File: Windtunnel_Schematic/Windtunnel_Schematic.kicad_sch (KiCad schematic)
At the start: 8 parts

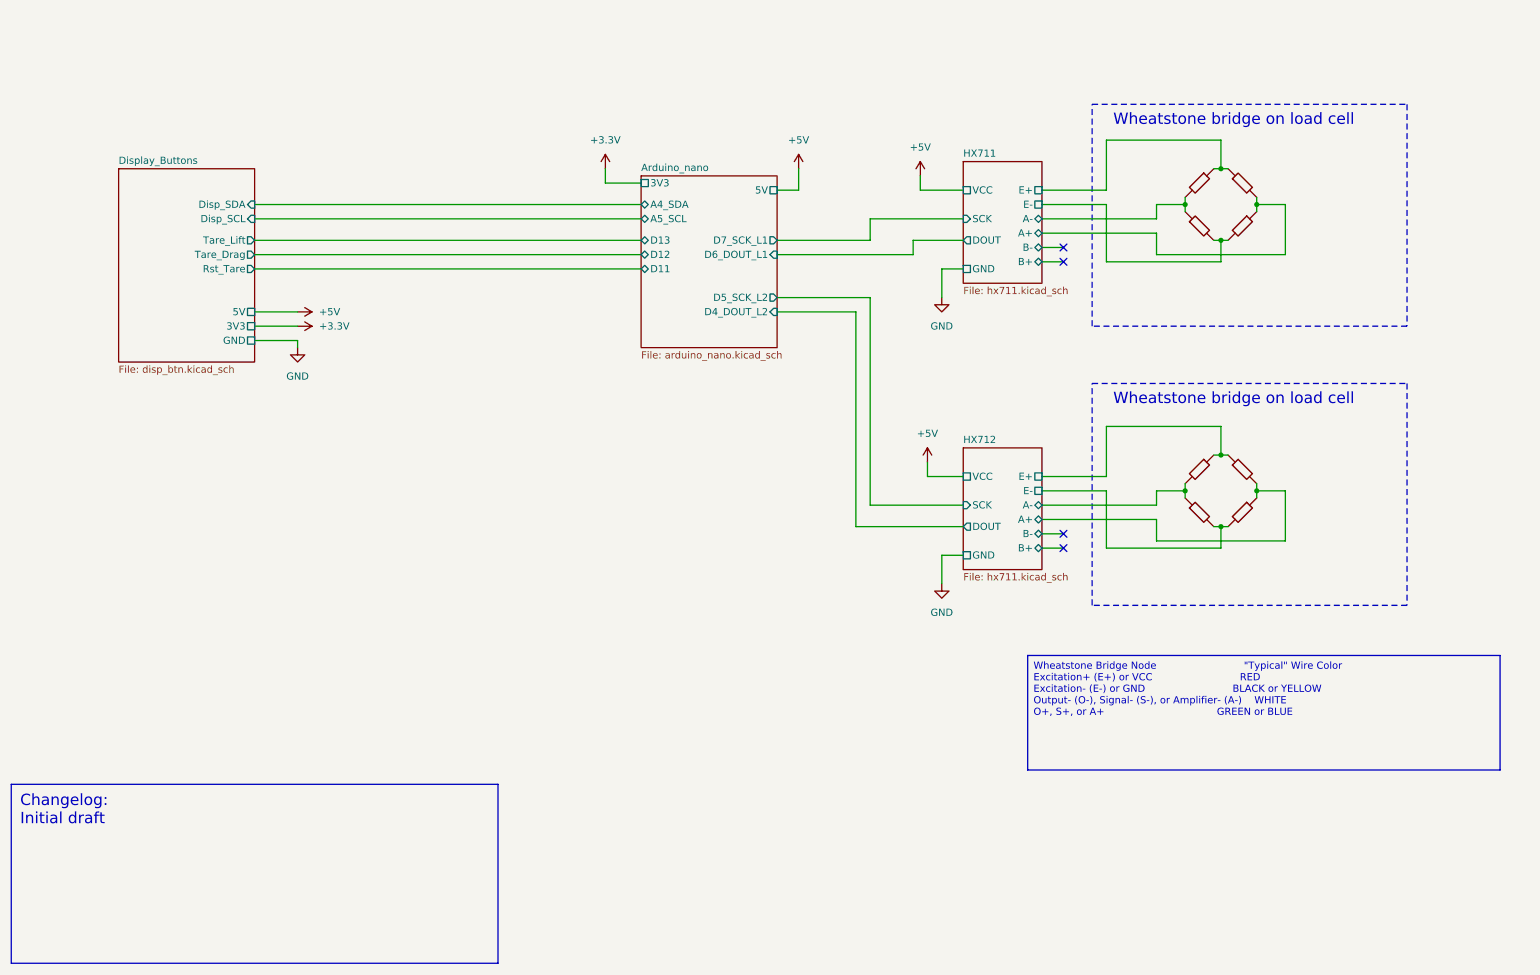
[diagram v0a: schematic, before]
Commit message: Added sub D9 and screw terminals
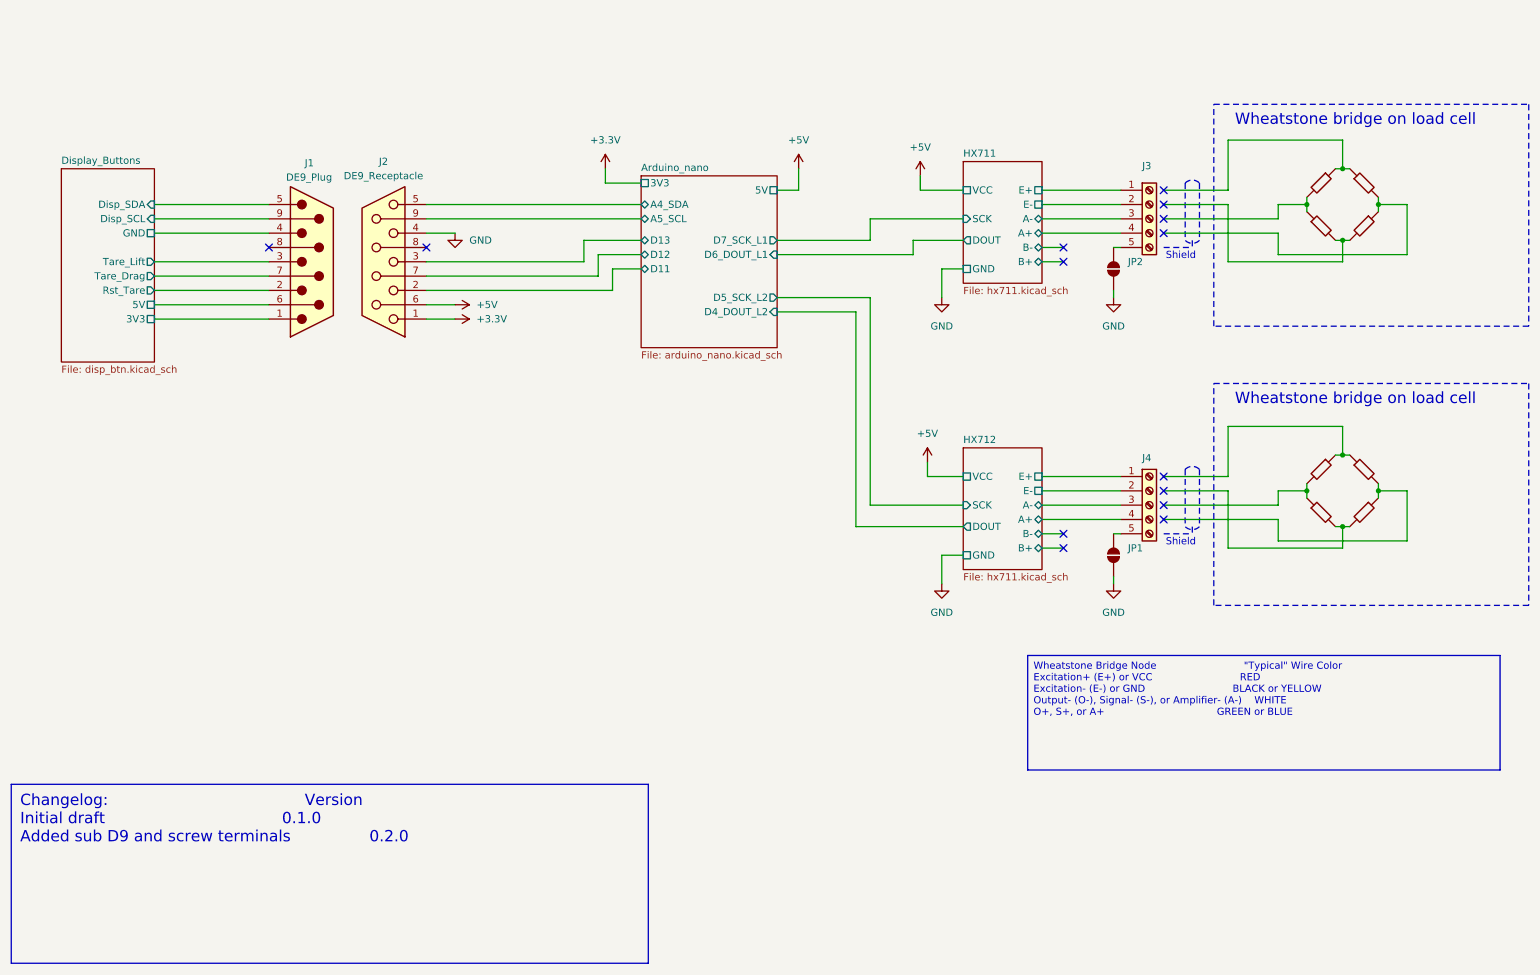
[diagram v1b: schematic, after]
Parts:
- added J1: DE9_Plug, symbol Connector:DE9_Plug
- added J2: DE9_Receptacle, symbol Connector:DE9_Receptacle
- added J3, J4: Screw_Terminal_01x05, TerminalBlock_Phoenix:TerminalBlock_Phoenix_MPT-0,5-5-2.54_1x05_P2.54mm_Horizontal, symbol Connector:Screw_Terminal_01x05
- added JP1, JP2: SolderJumper_2_Open, Jumper:SolderJumper-2_P1.3mm_Open_TrianglePad1.0x1.5mm, symbol Jumper:SolderJumper_2_Open
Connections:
- net +3.3V: now also J2.1
- net +5V: now also J2.6
- net Arduino_nano/A4_SDA: now also J2.5
- net Arduino_nano/A5_SCL: now also J2.9
- net Arduino_nano/D11: now also J2.2
- net Arduino_nano/D12: now also J2.7
- net Arduino_nano/D13: now also J2.3
- net GND: now also J2.4, JP1.1 (A), JP2.1 (A)
- net HX711/A+: now also J3.4 (Pin_4); no longer R2.2, R4.1
- net HX711/A-: now also J3.3 (Pin_3); no longer R1.2, R3.1
- net HX711/E+: now also J3.1 (Pin_1); no longer R1.1, R2.1
- net HX711/E-: now also J3.2 (Pin_2); no longer R3.2, R4.2
- net HX712/A+: now also J4.4 (Pin_4); no longer R7.2, R8.1
- net HX712/A-: now also J4.3 (Pin_3); no longer R5.2, R6.1
- net HX712/E+: now also J4.1 (Pin_1); no longer R5.1, R7.1
- net HX712/E-: now also J4.2 (Pin_2); no longer R6.2, R8.2
- new net: R1.2, R3.1
- new net: R3.2, R4.2
- new net: R1.1, R2.1
- new net: R2.2, R4.1
- new net: J3.5 (Pin_5), JP2.2 (B)
- new net: R5.1, R7.1
- new net: R7.2, R8.1
- new net: J4.5 (Pin_5), JP1.2 (B)
- new net: R6.2, R8.2
- new net: R5.2, R6.1
- new net Display_Buttons/3V3: J1.1
- new net Display_Buttons/5V: J1.6
- new net Display_Buttons/Disp_SCL: J1.9
- new net Display_Buttons/Disp_SDA: J1.5
- new net Display_Buttons/GND: J1.4
- new net Display_Buttons/Rst_Tare: J1.2
- new net Display_Buttons/Tare_Drag: J1.7
- new net Display_Buttons/Tare_Lift: J1.3
- no-connect marks 4 -> 14
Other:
- note added: "Shield"

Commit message: Schematic to 0.3.0 Nearly finished Trying to mill it tomorrow
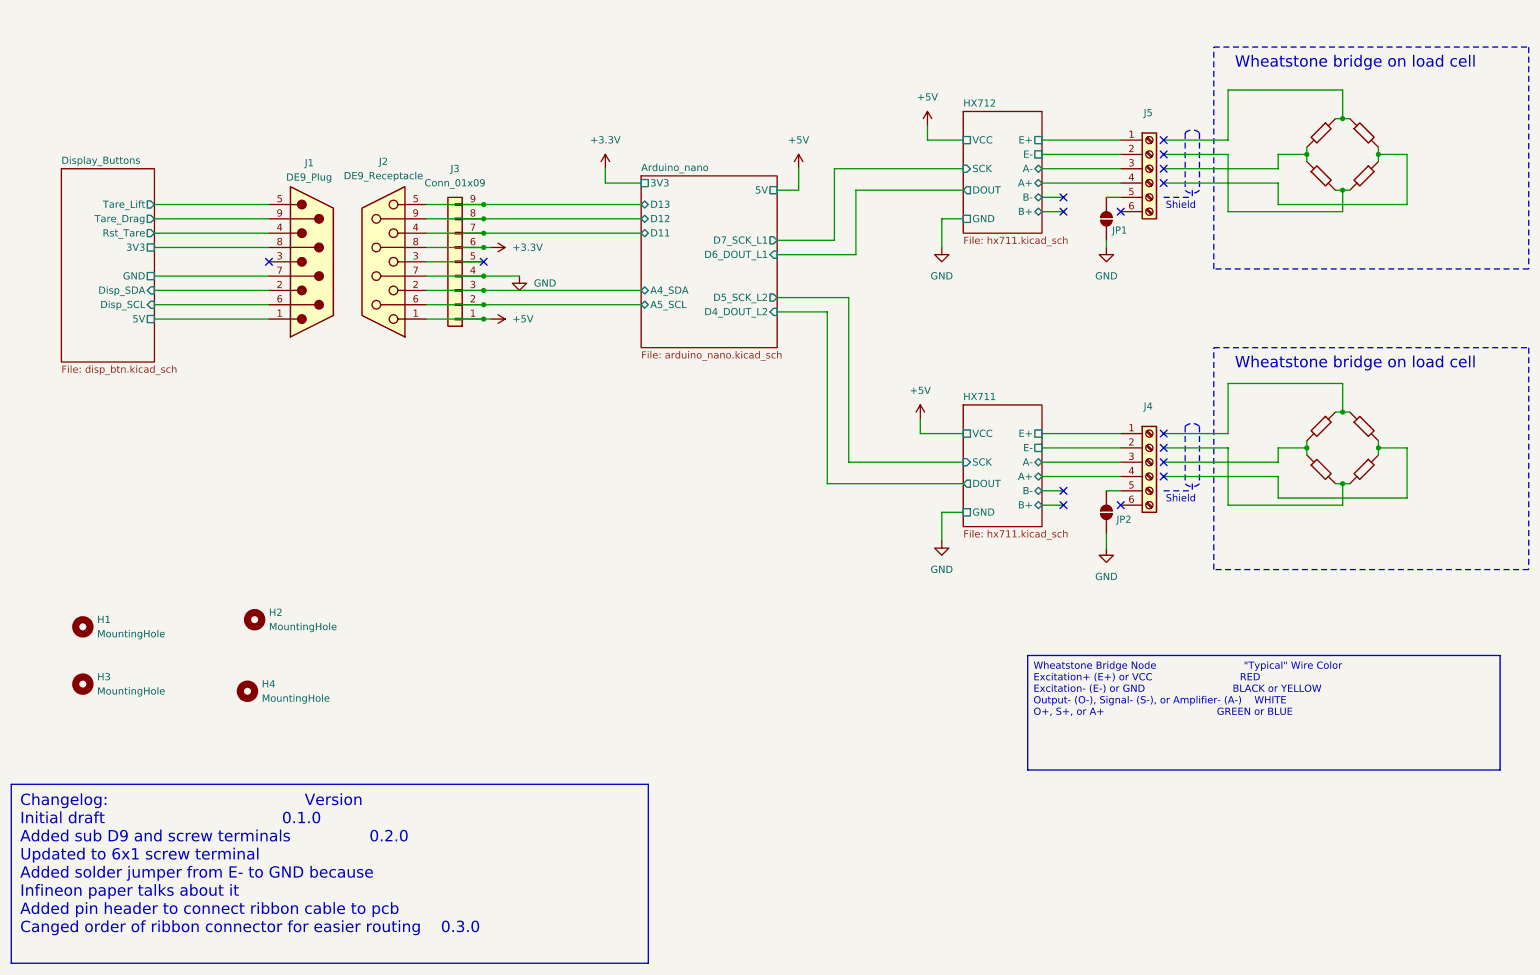
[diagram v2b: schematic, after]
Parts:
- removed J3, J4: Screw_Terminal_01x05, TerminalBlock_Phoenix:TerminalBlock_Phoenix_MPT-0,5-5-2.54_1x05_P2.54mm_Horizontal, symbol Connector:Screw_Terminal_01x05
- added H1, H2, H3, H4: MountingHole, MountingHole:MountingHole_4.3mm_M4, symbol Mechanical:MountingHole
- added J3: Conn_01x09, Connector_PinHeader_2.54mm:PinHeader_1x09_P2.54mm_Horizontal, symbol Connector_Generic:Conn_01x09
- added J4, J5: Screw_Terminal_01x06, TerminalBlock_Phoenix:TerminalBlock_Phoenix_MKDS-1,5-6_1x06_P5.00mm_Horizontal, symbol Connector:Screw_Terminal_01x06
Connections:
- net +3.3V: now also J2.8, J3.6 (Pin_6); no longer J2.1
- net +5V: now also J2.1, J3.1 (Pin_1); no longer J2.6
- net Arduino_nano/A4_SDA: now also J2.2, J3.3 (Pin_3); no longer J2.5
- net Arduino_nano/A5_SCL: now also J2.6, J3.2 (Pin_2); no longer J2.9
- net Arduino_nano/D11: now also J2.4, J3.7 (Pin_7); no longer J2.2
- net Arduino_nano/D12: now also J2.9, J3.8 (Pin_8); no longer J2.7
- net Arduino_nano/D13: now also J2.5, J3.9 (Pin_9); no longer J2.3
- net Display_Buttons/3V3: now also J1.8; no longer J1.1
- net Display_Buttons/5V: now also J1.1; no longer J1.6
- net Display_Buttons/Disp_SCL: now also J1.6; no longer J1.9
- net Display_Buttons/Disp_SDA: now also J1.2; no longer J1.5
- net Display_Buttons/GND: now also J1.7; no longer J1.4
- net Display_Buttons/Rst_Tare: now also J1.4; no longer J1.2
- net Display_Buttons/Tare_Drag: now also J1.9; no longer J1.7
- net Display_Buttons/Tare_Lift: now also J1.5; no longer J1.3
- net GND: now also J2.7, J3.4 (Pin_4); no longer J2.4
- net HX711/A+: now also J4.4 (Pin_4)
- net HX711/A-: now also J4.3 (Pin_3)
- net HX711/E+: now also J4.1 (Pin_1)
- net HX711/E-: now also J4.2 (Pin_2)
- net HX712/A+: now also J5.4 (Pin_4)
- net HX712/A-: now also J5.3 (Pin_3)
- net HX712/E+: now also J5.1 (Pin_1)
- net HX712/E-: now also J5.2 (Pin_2)
- net at JP2.2 (B): now also J4.5 (Pin_5)
- net at JP1.2 (B): now also J5.5 (Pin_5)
- new net: J2.3, J3.5 (Pin_5)
- no-connect marks 14 -> 16
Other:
- moved on the sheet: JP1, JP2

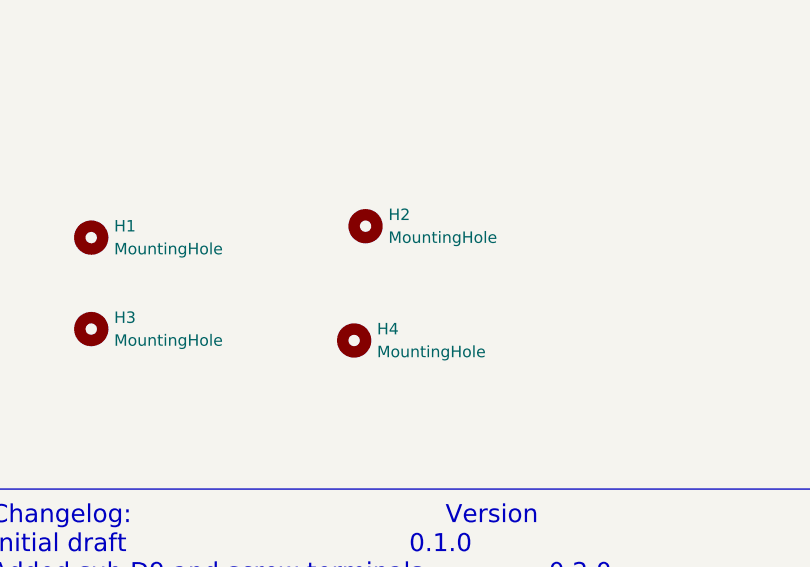
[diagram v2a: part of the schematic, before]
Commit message: Schematic: First version is done and working TODO: Add labling to pcb Add comments Add changes for next version, but we will not manufacture this one
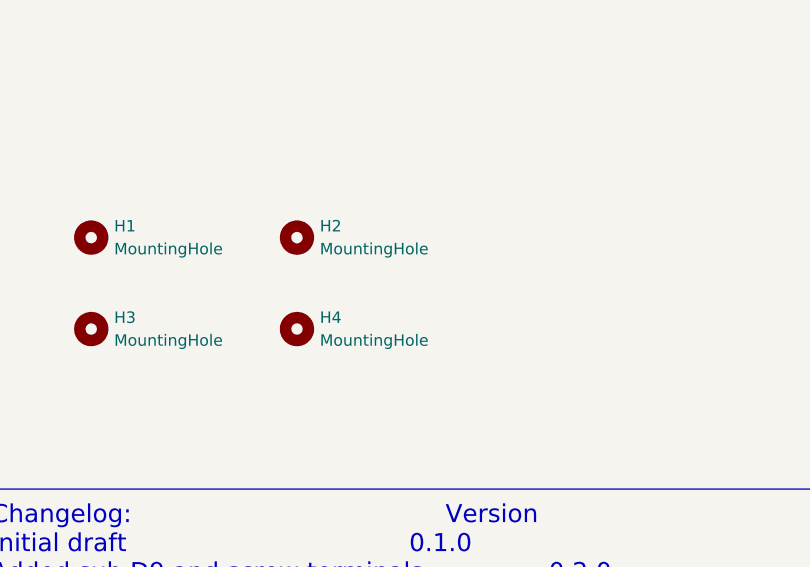
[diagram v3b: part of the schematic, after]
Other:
- moved on the sheet: H2, H4
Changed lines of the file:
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@@
 	(symbol
 		(lib_id "Mechanical:MountingHole")
-		(at 57.15 134.62 0)
+		(at 49.53 135.89 0)
 		(unit 1)
 		(exclude_from_sim yes)
@@
 		(fields_autoplaced yes)
 		(property "Reference" "H2"
-			(at 59.69 133.3499 0)
+			(at 52.07 134.6199 0)
 			(effects
 				(font
@@
 		)
 		(property "Value" "MountingHole"
-			(at 59.69 135.8899 0)
+			(at 52.07 137.1599 0)
 			(effects
 				(font
@@
 		)
 		(property "Footprint" "MountingHole:MountingHole_4.3mm_M4"
-			(at 57.15 134.62 0)
+			(at 49.53 135.89 0)
 			(effects
 				(font
@@
 		)
 		(property "Datasheet" "~"
-			(at 57.15 134.62 0)
+			(at 49.53 135.89 0)
 			(effects
 				(font
@@
 		)
 		(property "Description" "Mounting Hole without connection"
-			(at 57.15 134.62 0)
+			(at 49.53 135.89 0)
 			(effects
 				(font
@@
 	(symbol
 		(lib_id "Mechanical:MountingHole")
-		(at 55.88 147.32 0)
+		(at 49.53 146.05 0)
 		(unit 1)
 		(exclude_from_sim yes)
@@
 		(fields_autoplaced yes)
 		(property "Reference" "H4"
-			(at 58.42 146.0499 0)
+			(at 52.07 144.7799 0)
 			(effects
 				(font
@@
 		)
 		(property "Value" "MountingHole"
-			(at 58.42 148.5899 0)
+			(at 52.07 147.3199 0)
 			(effects
 				(font
@@
 		)
 		(property "Footprint" "MountingHole:MountingHole_4.3mm_M4"
-			(at 55.88 147.32 0)
+			(at 49.53 146.05 0)
 			(effects
 				(font
@@
 		)
 		(property "Datasheet" "~"
-			(at 55.88 147.32 0)
+			(at 49.53 146.05 0)
 			(effects
 				(font
@@
 		)
 		(property "Description" "Mounting Hole without connection"
-			(at 55.88 147.32 0)
-			(effects
-				(font
+			(at 49.53 146.05 0)
+			(effects
+				(font

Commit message: Add to docs, schematic and general calculation: ADD prototype data Change Schematic revision to 0.4.0 ADD requirements.txt for each general calculation virtual environment
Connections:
- net Arduino_nano/D11 renamed Arduino_nano/D10_Rst_Tare
- net Arduino_nano/D12 renamed Arduino_nano/D11_Tare_Drag
- net Arduino_nano/D13 renamed Arduino_nano/D12_Tare_Lift
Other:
- sheet Arduino_nano ports: added D10_Rst_Tare, D11_Tare_Drag, D12_Tare_Lift; removed D11, D12, D13
- note added: "Drag"
- note added: "Lift"
- moved on the sheet: J1, J2, J3, J4, J5, JP1, JP2
